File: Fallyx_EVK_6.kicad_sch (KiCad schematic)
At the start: 25 parts, among them J5 MTSW-101-X-X-D-X, J6 USB_C_6P, U1 XC9236F08CER-G, U6 MCP73831T-2ACI_OT, U7 BQ27421YZFR-G1A

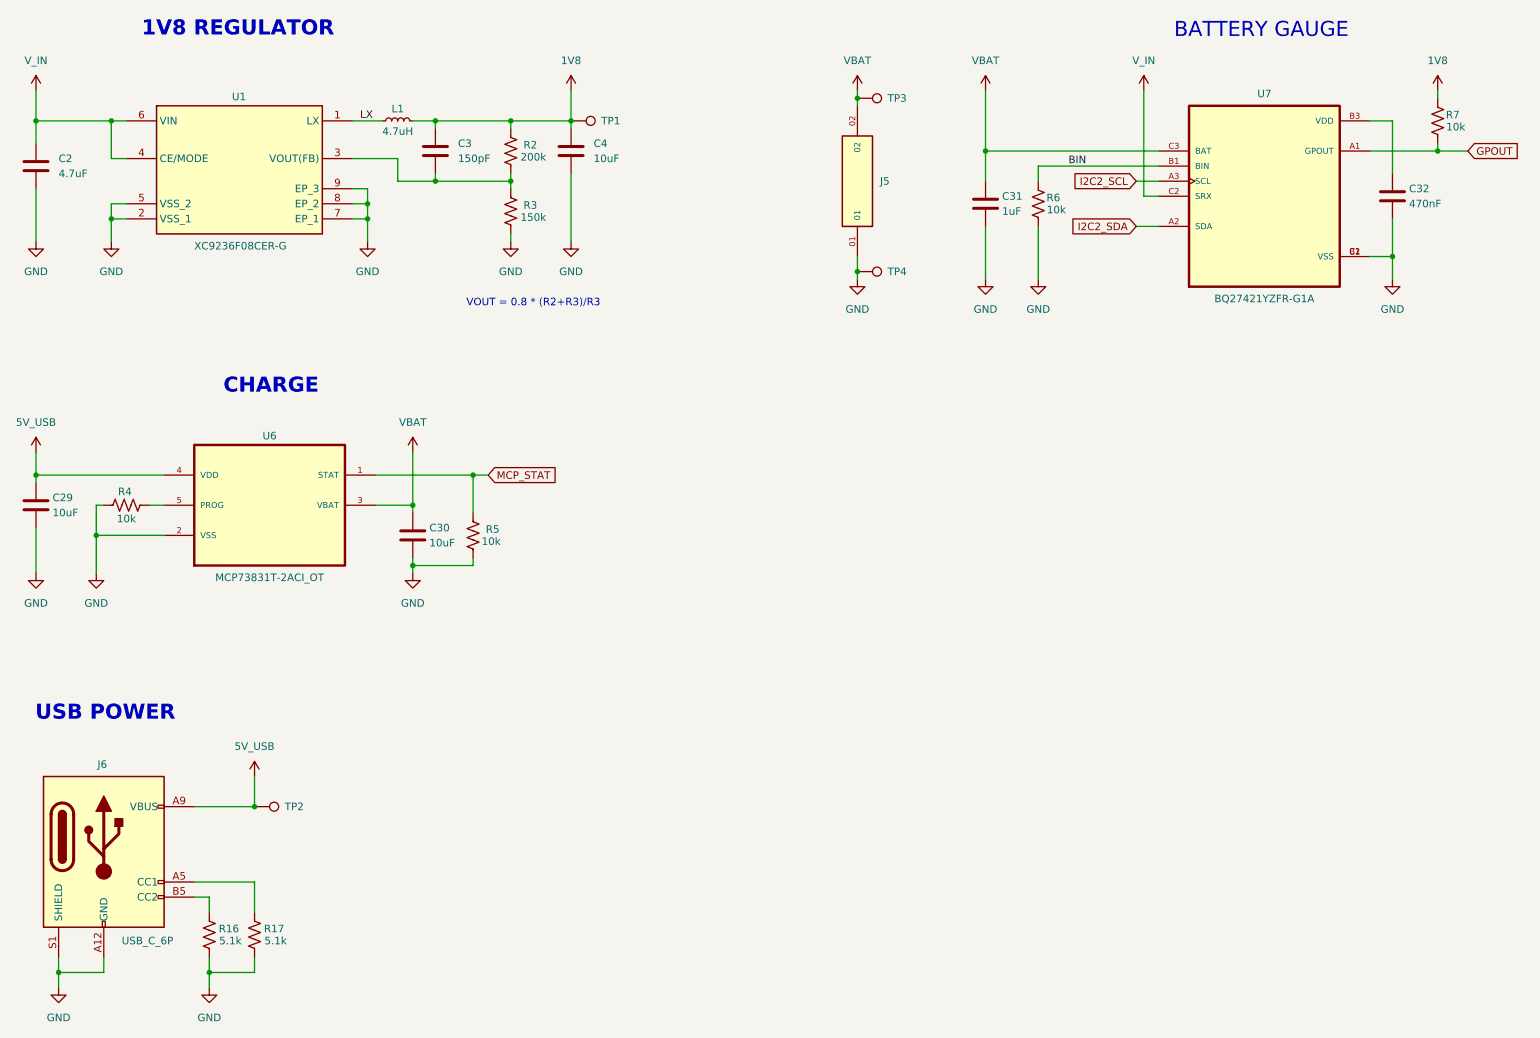
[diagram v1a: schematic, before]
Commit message: Updated for new BLE modules
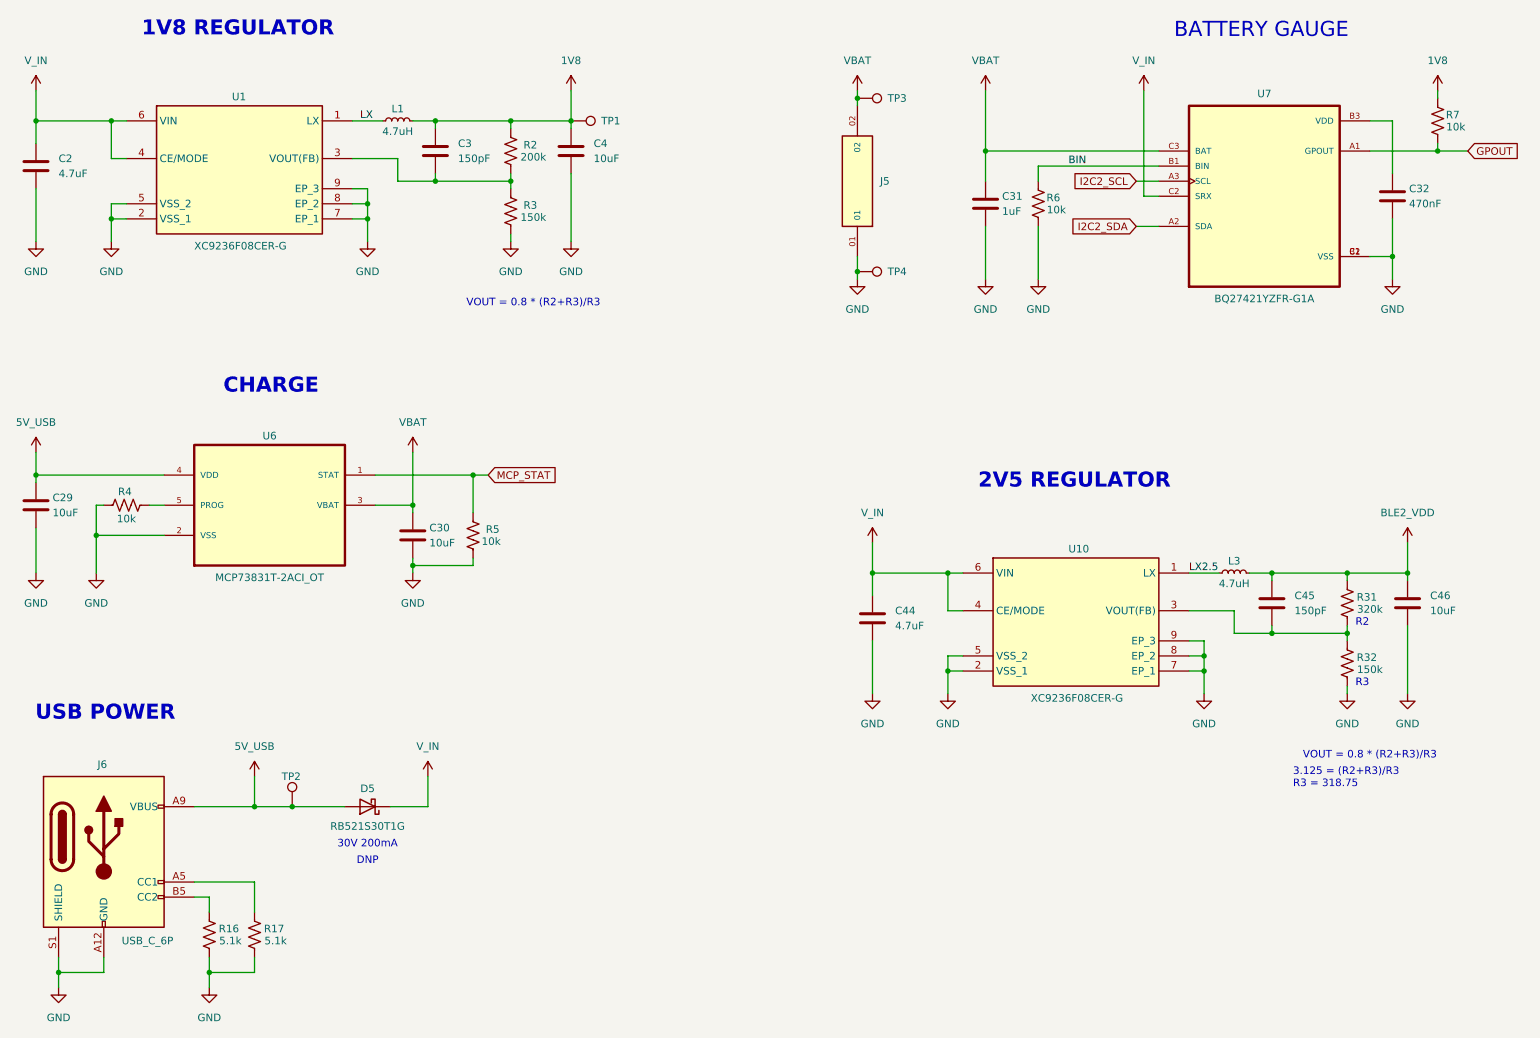
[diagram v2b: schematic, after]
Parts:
- added C44: 4.7uF, Capacitor_SMD:C_0603_1608Metric, symbol Device:C
- added C45: 150pF, Capacitor_SMD:C_0603_1608Metric, symbol Device:C
- added C46: 10uF, Capacitor_SMD:C_0805_2012Metric, symbol Device:C
- added D5: RB521S30T1G, RB521S30T1G:DIOM168X70N, symbol Device:D_Schottky
- added L3: 4.7uH, NR3015T4R7M:IND_TAIYO_NR3015_TAY, symbol Device:L_Small
- added R31: 320k, Resistor_SMD:R_0402_1005Metric, symbol Device:R_US
- added R32: 150k, Resistor_SMD:R_0402_1005Metric, symbol Device:R_US
- added U10: XC9236F08CER-G, XC9236F08CERG, symbol XC9236F08CER-G:XC9236F08CER-G
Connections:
- net 5V_USB: now also D5.2 (A)
- net GND: now also C44.2, C46.2, R32.1, U10.2 (VSS_1), U10.5 (VSS_2), U10.7 (EP_1), U10.8 (EP_2), U10.9 (EP_3)
- net V_IN: now also C44.1, D5.1 (K), U10.4 (CE/MODE), U10.6 (VIN)
- new net: C45.2, R31.1, R32.2, U10.3 (VOUT(FB))
- new net BLE2_VDD: C45.1, C46.1, L3.2, R31.2
- new net LX2.5: L3.1, U10.1 (LX)
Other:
- note added: "2V5 REGULATOR"
- note added: "3.125 = (R2+R3)/R3 R3 = 318.75"
- note added: "30V 200mA"
- note added: "DNP"
- note added: "R2"
- note added: "R3"
- moved on the sheet: TP2

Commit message: Final Routing and export for EVK
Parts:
- R31: value 320k -> 330k
- R32: value 150k -> 160k
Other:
- note added: "3.125 = (R2+R3)/R3 R3 = 160 R2 = 330"
- note removed: "3.125 = (R2+R3)/R3 R3 = 318.75"
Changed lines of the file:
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@@
 		)
 	)
-	(text "3.125 = (R2+R3)/R3\nR3 = 318.75"
+	(text "3.125 = (R2+R3)/R3\nR3 = 160\nR2 = 330"
 		(exclude_from_sim no)
 		(at 238.506 150.114 0)
@@
 			)
 		)
-		(property "Value" "150k"
+		(property "Value" "160k"
 			(at 251.46 131.826 0)
 			(effects
@@
 			)
 		)
-		(property "Value" "320k"
+		(property "Value" "330k"
 			(at 251.46 121.666 0)
 			(effects
